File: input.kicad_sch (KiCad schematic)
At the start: 8 parts, among them J1 USB_C_16P, U1 CH224K

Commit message: sourcing: lock LCSC + MPN + Manufacturer + Footprint for every remaining BOM line
Applied JLCPCB picks (LCSC number + manufacturer part number + tuned
footprint) across all four sub-sheets — 72 components total.  Every
placed component now carries LCSC, MPN, and Manufacturer properties;
the built-in Value/Footprint fields point to the exact JLCPCB stock
unit for that pick.

Highlights:
- ICs (Preferred where available, Extended otherwise):
    U1(bms)      BQ7692003PWR   C601650    TSSOP-20
    U1(charger)  IP2326         C2832094   VQFN-24 EP4x4
    U1(input)    CH224K         C970725    ESSOP-10
    U1(bckbst)   LM5176PWPR     C442493    HTSSOP-28
- Diodes + TVS (all Preferred tier):
    D1(input)    SRV05-4        C7420376   SOT-23-6   (622K stock)
    D2(input)    SMAJ12A        C19077531  SMA        ( 33K stock)
    D1-3(bms)    SMAJ15A        C19077535  SMA        (174K stock)
- Power passives:
    L1(bckbst)   6.8uH 5A       C167221    FXL0630-6R8-M  7x6.6mm
    L1(charger)  2.2uH 4.8A     C602029    FHD4020S-2R2MT 4x4mm
    FB1(input)   600R@100MHz    C139183    CBW160808U601T 0603 (1A)
    R9(bms)      5mR 2W ±1%     C185817    RLM25FEER005   2512
- Bulk passives — Uniohm 0603WAF series, ±1%, high stock.  All caps
  Samsung/Yageo 0603 or 0805 ceramic.  Reused Q1-Q4 = AON7544
  (already locked at 9120877) for bms.Q1/Q2 too — same part
  covers 30V/20A pack-return FET stack.

Effect on pre-fab readiness (kicad-happy):
- SS-001 error CLEARED — 1/34 MPN coverage was blocking pre-fab;
  now 34/34 (100%).
- DS-002 warning shifted: was "no datasheets" (2/34 MPNs), now
  "no datasheets dir" (34/34 MPNs).  Non-blocking; datasheet PDFs
  are nice-to-have but the review can proceed without them.
- 1 remaining error PP-001 (LM5176_VCC no DC source) is a false
  positive: KiCad library symbol declares VCC as power_in but it's
  actually the LM5176's internal 5V LDO OUTPUT.  Accepted as-is.

Full-project ERC still 0 errors.  Schematic is now sourcing-clean
and ready for 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
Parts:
- C1, C2: LCSC (none) -> C15850; MPN (none) -> CL21A106KAYNNNE; Manufacturer (none) -> SAMSUNG
- D1: footprint (none) -> Package_TO_SOT_SMD:SOT-23-6; LCSC (none) -> C7420376; MPN (none) -> SRV05-4; Manufacturer (none) -> HSMC
- D2: footprint (none) -> Diode_SMD:D_SMA; LCSC (none) -> C19077531; MPN (none) -> SMAJ12A; Manufacturer (none) -> LRC
- FB1: footprint (none) -> Inductor_SMD:L_0603_1608Metric; LCSC (none) -> C139183; MPN (none) -> CBW160808U601T; Manufacturer (none) -> Sunlord
- J1: footprint (none) -> Connector_USB:USB_C_Receptacle_HRO_TYPE-C-31-M-12; LCSC (none) -> C709357; MPN (none) -> KH-TYPE-C-16P; Manufacturer (none) -> Korean Hroparts
- R1: LCSC (none) -> C23352; MPN (none) -> 0603WAF2402T5E; Manufacturer (none) -> Uniohm
- U1: footprint (none) -> Package_SO:SSOP-10-1EP_3.9x4.9mm_P1mm_EP2.1x3.3mm; LCSC (none) -> C970725; MPN (none) -> CH224K; Manufacturer (none) -> WCH

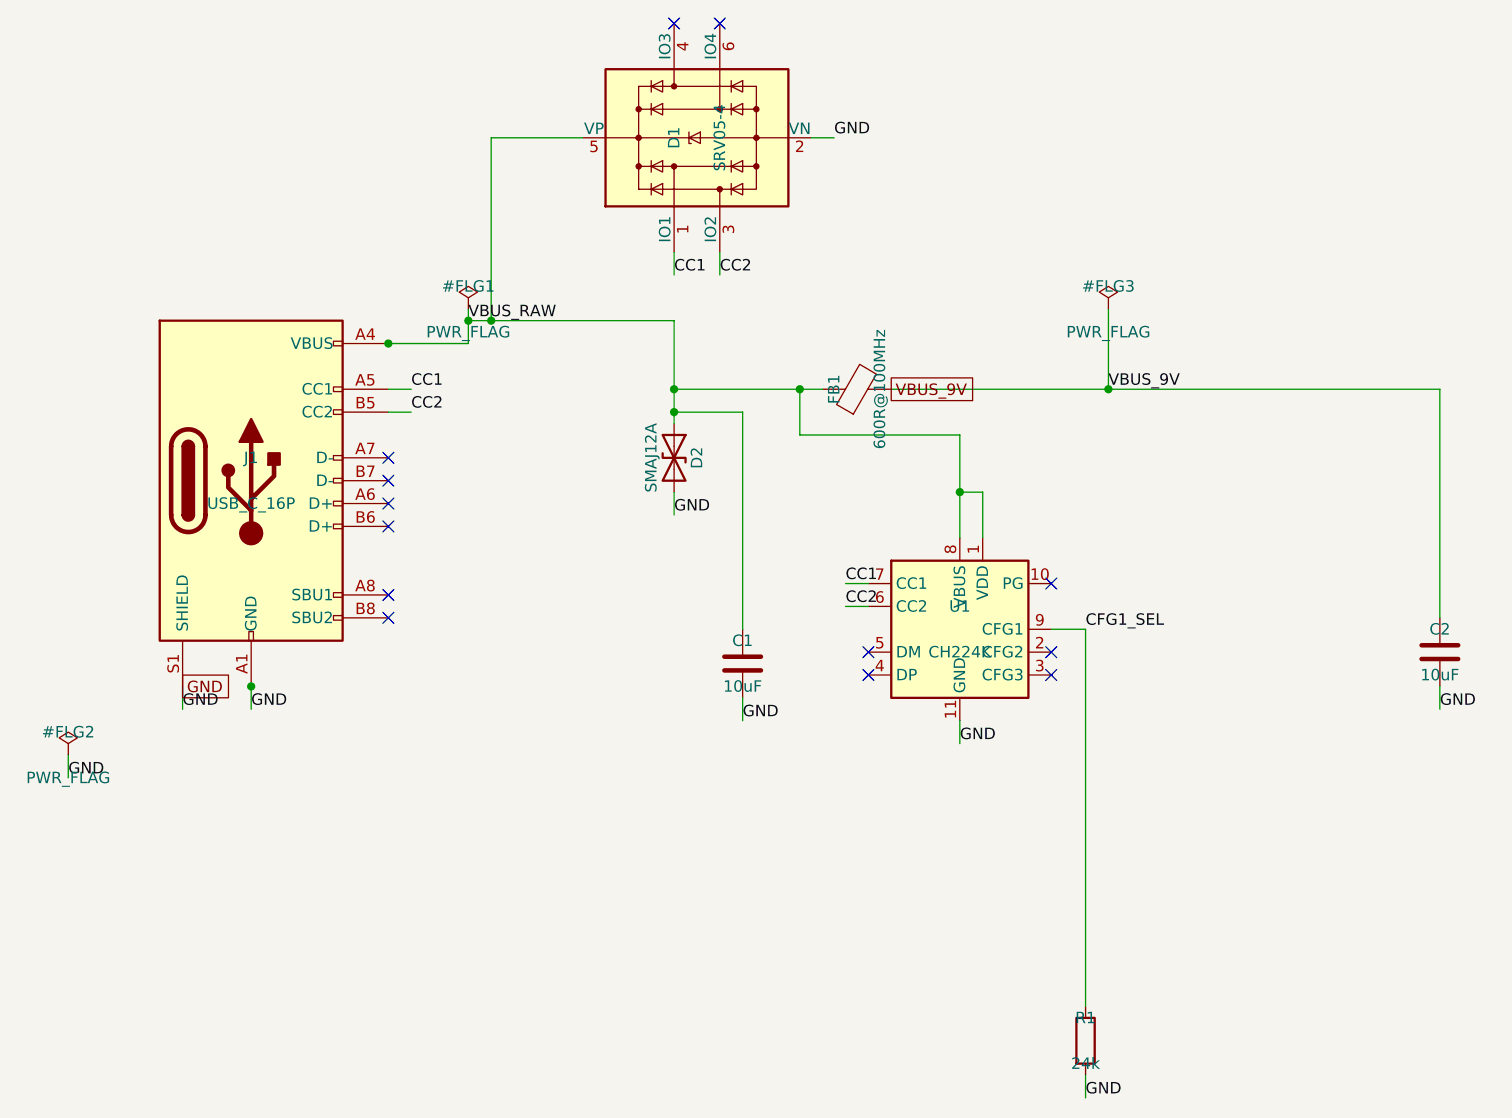
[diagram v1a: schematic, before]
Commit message: sheets: hierarchical ref disambiguation via annotate_schematic
Every sub-sheet symbol now carries a `_{SHEETNAME}{instance_num}` suffix so
refs are globally unique across the hierarchy.  76 refs rewritten:
  bms:       27 (e.g. U1 → U1_BMS1,      Q1 → Q1_BMS1)
  charger:   19 (e.g. U1 → U1_CHARGER1,  R7 → R7_CHARGER1)
  input:      8 (e.g. U1 → U1_INPUT1,    J1 → J1_INPUT1)
  buckboost: 22 (e.g. U1 → U1_BUCKBOOST1,Q1 → Q1_BUCKBOOST1)

Fixes kicad-cli's `schematic has annotation errors` warning which previously
caused BOM export to collapse the four different U1's (BQ76920 + IP2326 +
CH224K + LM5176) into a single row with comma-joined values.

bom_step1.csv committed alongside as the post-disambiguation baseline —
38 grouped rows, 100% LCSC/MPN coverage.

Applied via the new `annotate_schematic` hierarchical pass shipped in
KiCAD-MCP-Server c529efa on develop.  See NOTES.md for the mid-session
handoff block and memory `feedback_hierarchical_annotate`.

Co-Authored-By: Claude Opus 4.7 <noreply@anthropic.com>
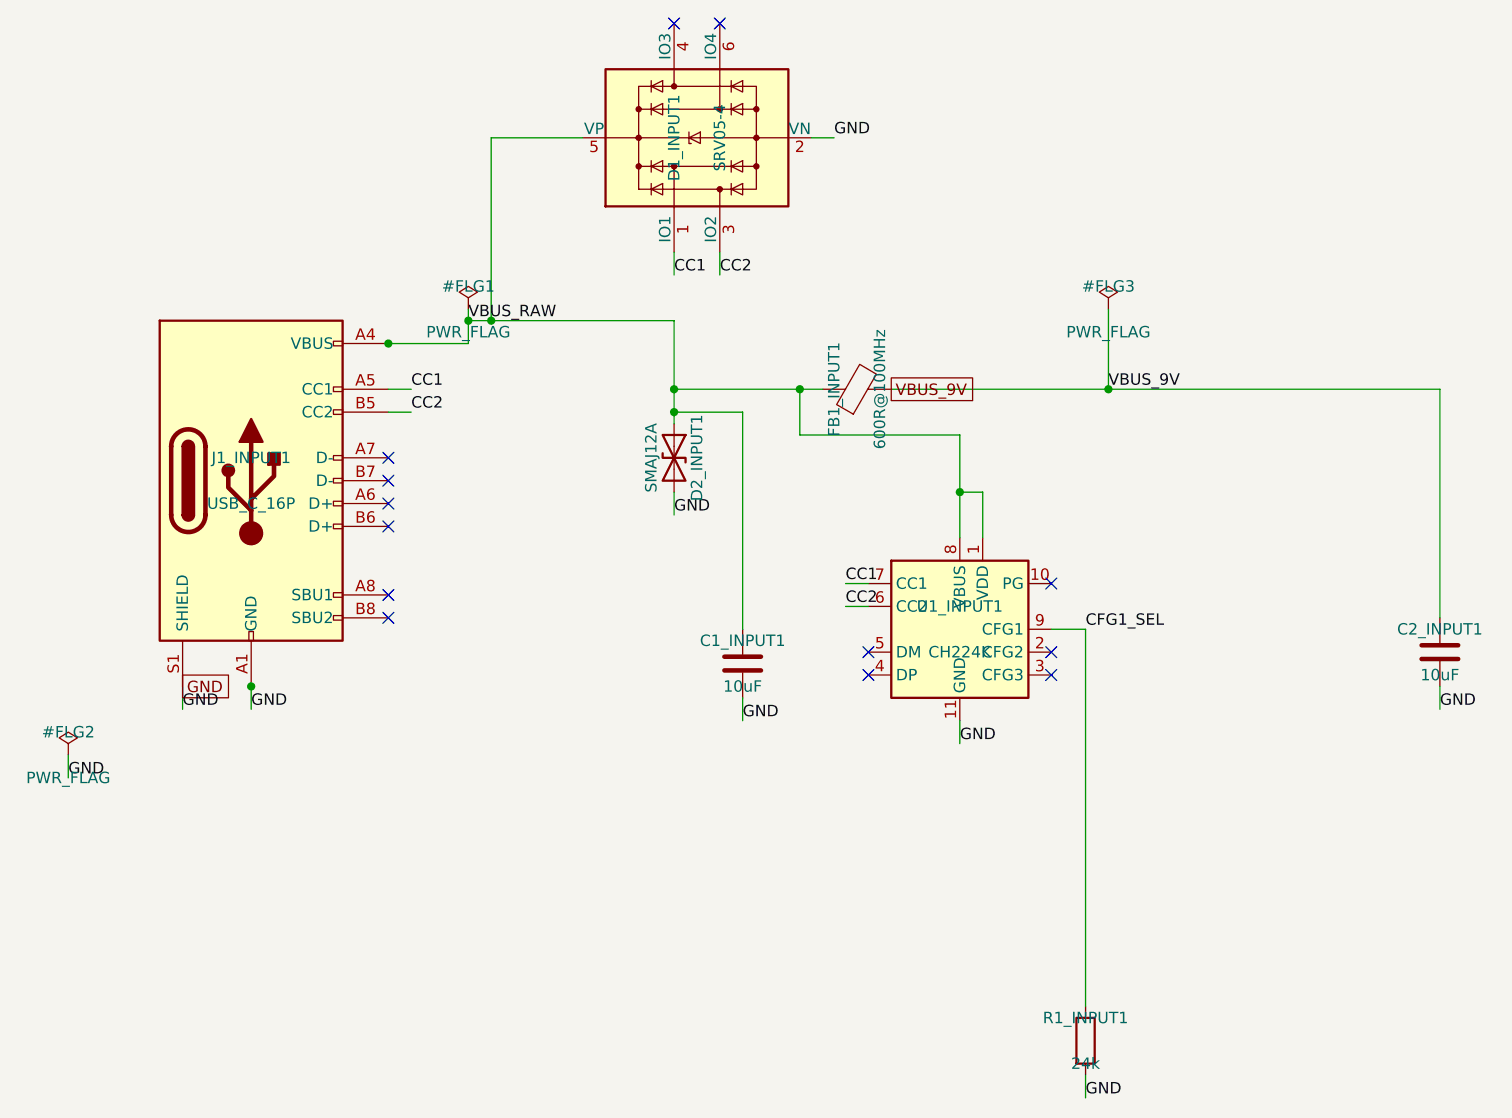
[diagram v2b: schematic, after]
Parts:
- renumbered C1 to C1_INPUT1, C2 to C2_INPUT1, D1 to D1_INPUT1, D2 to D2_INPUT1, FB1 to FB1_INPUT1, J1 to J1_INPUT1, R1 to R1_INPUT1, U1 to U1_INPUT1

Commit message: Step 2: complete Footprint set + sync 76 footprints to .kicad_pcb
Fill in the Footprint properties that were missing from the prior
sourcing pass, and sync everything to the PCB.

Footprint updates on the schematic:
- 35 passives got their Footprint assigned by value (0603 for R/C ≤1uF,
  0805 for 10uF/22uF caps).
- BAT1_BMS1 → power_module_lib:BAT-SMD_BH-18650-B5BA016 (was truncated).
- L1_BUCKBOOST1 → Inductor_SMD:L_Sumida_CDMC6D28_7.25x6.5mm (needed the
  size suffix so KiCad can resolve the .kicad_mod file).

Sync result: 76/76 footprints imported, 60 nets added, 245 pads assigned,
0 import errors.  Unmatched pads reported are all intentional NCs per
REQUIREMENTS.md (USB-C D+/D-, CH224K SBU/CFG, SRV05-4 unused ESD channels).

The footprints are at the default y=-140..-20 auto-import grid; no
placement work yet.  Next step is add_board_outline + set_design_rules.

For discoverability going forward, the pre-sync gap gets caught by
check_sourcing_readiness (KiCAD-MCP-Server fa93ba9 on develop) rather
than having to reset the .kicad_pcb after every retro-fill of an empty
Footprint property.

Co-Authored-By: Claude Opus 4.7 <noreply@anthropic.com>
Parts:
- C1_INPUT1, C2_INPUT1: footprint (none) -> Capacitor_SMD:C_0805_2012Metric
- R1_INPUT1: footprint (none) -> Resistor_SMD:R_0603_1608Metric
